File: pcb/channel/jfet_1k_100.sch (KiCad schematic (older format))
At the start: 7 parts, among them Q15 2SK3557-7-TB-E

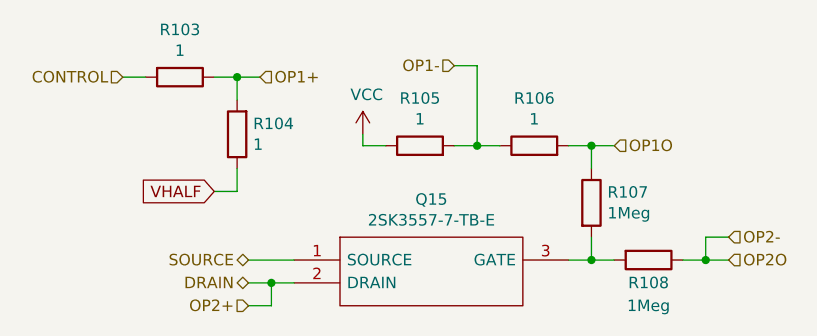
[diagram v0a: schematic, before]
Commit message: Reduce JFET base resistor from 1Meg to 100K
Precaution against too much voltage drop to base
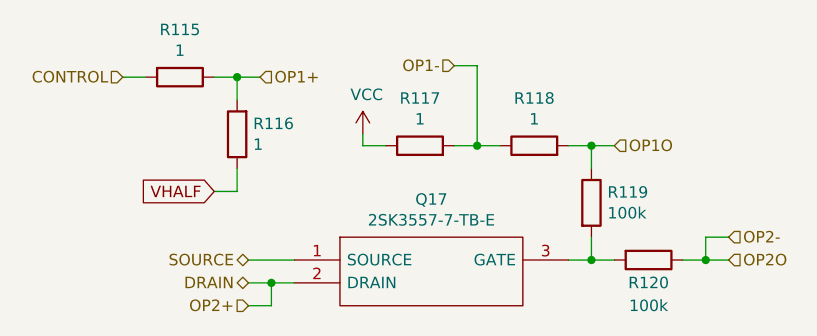
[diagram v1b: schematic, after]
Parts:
- R107, R108: value 1Meg -> 100k
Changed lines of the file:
@@
 $Descr A4 11693 8268
 encoding utf-8
-Sheet 17 19
+Sheet 18 19
 Title ""
 Date ""
@@
 Comment4 ""
 $EndDescr
-Wire Wire Line
-	6500 3950 6400 3950
-$Comp
-L Device:R R?
-U 1 1 5F3CFF6E
-P 6250 3950
-AR Path="/5F23B5B7/5F329280/5F32989F/5F3CFF6E" Ref="R?"  Part="1"
-AR Path="/5F23B5B7/5F329280/5F359E3D/5F3CFF6E" Ref="R?"  Part="1"
-AR Path="/5F23B5B7/5F329280/5F36404F/5F3CFF6E" Ref="R?"  Part="1"
-AR Path="/5F23B5B7/5F53A760/5F32989F/5F3CFF6E" Ref="R?"  Part="1"
-AR Path="/5F23B5B7/5F53A760/5F36404F/5F3CFF6E" Ref="R?"  Part="1"
-AR Path="/5F23B5B7/5F53A760/5F359E3D/5F3CFF6E" Ref="R?"  Part="1"
-AR Path="/5F23B5B7/5F53B8BF/5F32989F/5F3CFF6E" Ref="R?"  Part="1"
-AR Path="/5F23B5B7/5F53B8BF/5F36404F/5F3CFF6E" Ref="R?"  Part="1"
-AR Path="/5F23B5B7/5F53B8BF/5F359E3D/5F3CFF6E" Ref="R?"  Part="1"
-AR Path="/5F23B5B7/5F53BC28/5F32989F/5F3CFF6E" Ref="R?"  Part="1"
-AR Path="/5F23B5B7/5F53BC28/5F36404F/5F3CFF6E" Ref="R?"  Part="1"
-AR Path="/5F23B5B7/5F53BC28/5F359E3D/5F3CFF6E" Ref="R?"  Part="1"
-AR Path="/604ABC92/5F32989F/5F3CFF6E" Ref="R106"  Part="1"
-AR Path="/604ABC92/5F36404F/5F3CFF6E" Ref="R112"  Part="1"
-AR Path="/604ABC92/5F359E3D/5F3CFF6E" Ref="R118"  Part="1"
-F 0 "R106" V 6457 3950 50  0000 C CNN
-F 1 "1" V 6366 3950 50  0000 C CNN
-F 2 "Resistor_SMD:R_0603_1608Metric_Pad1.05x0.95mm_HandSolder" V 6180 3950 50  0001 C CNN
-F 3 "~" H 6250 3950 50  0001 C CNN
-	1    6250 3950
-	0    -1   -1   0
-$EndComp
-Wire Wire Line
-	6000 3950 6100 3950
-Connection ~ 6000 3950
 Wire Wire Line
 	5900 3950 6000 3950
@@
 AR Path="/604ABC92/5F36404F/5F3CF1A6" Ref="R111"  Part="1"
 AR Path="/604ABC92/5F359E3D/5F3CF1A6" Ref="R117"  Part="1"
-F 0 "R105" V 5957 3950 50  0000 C CNN
+F 0 "R117" V 5957 3950 50  0000 C CNN
 F 1 "1" V 5866 3950 50  0000 C CNN
 F 2 "Resistor_SMD:R_0603_1608Metric_Pad1.05x0.95mm_HandSolder" V 5680 3950 50  0001 C CNN
@@
 AR Path="/604ABC92/5F36404F/5F3D5B39" Ref="R114"  Part="1"
 AR Path="/604ABC92/5F359E3D/5F3D5B39" Ref="R120"  Part="1"
-F 0 "R108" V 6850 4450 50  0000 C CNN
-F 1 "1Meg" V 6950 4450 50  0000 C CNN
+F 0 "R120" V 6850 4450 50  0000 C CNN
+F 1 "100k" V 6950 4450 50  0000 C CNN
 F 2 "Resistor_SMD:R_0603_1608Metric_Pad1.05x0.95mm_HandSolder" V 6680 4450 50  0001 C CNN
 F 3 "~" H 6750 4450 50  0001 C CNN
@@
 Wire Wire Line
 	6500 4350 6500 4450
-$Comp
-L Device:R R?
-U 1 1 5F3D481C
-P 6500 4200
-AR Path="/5F23B5B7/5F329280/5F32989F/5F3D481C" Ref="R?"  Part="1"
-AR Path="/5F23B5B7/5F329280/5F359E3D/5F3D481C" Ref="R?"  Part="1"
-AR Path="/5F23B5B7/5F329280/5F36404F/5F3D481C" Ref="R?"  Part="1"
-AR Path="/5F23B5B7/5F53A760/5F32989F/5F3D481C" Ref="R?"  Part="1"
-AR Path="/5F23B5B7/5F53A760/5F36404F/5F3D481C" Ref="R?"  Part="1"
-AR Path="/5F23B5B7/5F53A760/5F359E3D/5F3D481C" Ref="R?"  Part="1"
-AR Path="/5F23B5B7/5F53B8BF/5F32989F/5F3D481C" Ref="R?"  Part="1"
-AR Path="/5F23B5B7/5F53B8BF/5F36404F/5F3D481C" Ref="R?"  Part="1"
-AR Path="/5F23B5B7/5F53B8BF/5F359E3D/5F3D481C" Ref="R?"  Part="1"
-AR Path="/5F23B5B7/5F53BC28/5F32989F/5F3D481C" Ref="R?"  Part="1"
-AR Path="/5F23B5B7/5F53BC28/5F36404F/5F3D481C" Ref="R?"  Part="1"
-AR Path="/5F23B5B7/5F53BC28/5F359E3D/5F3D481C" Ref="R?"  Part="1"
-AR Path="/604ABC92/5F32989F/5F3D481C" Ref="R107"  Part="1"
-AR Path="/604ABC92/5F36404F/5F3D481C" Ref="R113"  Part="1"
-AR Path="/604ABC92/5F359E3D/5F3D481C" Ref="R119"  Part="1"
-F 0 "R107" H 6570 4246 50  0000 L CNN
-F 1 "1Meg" H 6570 4155 50  0000 L CNN
-F 2 "Resistor_SMD:R_0603_1608Metric_Pad1.05x0.95mm_HandSolder" V 6430 4200 50  0001 C CNN
-F 3 "~" H 6500 4200 50  0001 C CNN
-	1    6500 4200
-	1    0    0    -1
-$EndComp
-Connection ~ 6500 3950
-Wire Wire Line
-	6500 4050 6500 3950
-Wire Wire Line
-	6600 3950 6500 3950
 $Comp
 L 2SK3557-7-TB-E:2SK3557-7-TB-E Q?
@@
 AR Path="/604ABC92/5F36404F/5F3D9719" Ref="Q16"  Part="1"
 AR Path="/604ABC92/5F359E3D/5F3D9719" Ref="Q17"  Part="1"
-F 0 "Q15" H 5800 4715 50  0000 C CNN
+F 0 "Q17" H 5800 4715 50  0000 C CNN
 F 1 "2SK3557-7-TB-E" H 5800 4624 50  0000 C CNN
 F 2 "footprints:SOT95P250X135-3N" H 6250 4550 50  0001 L CNN
@@
 AR Path="/604ABC92/5F36404F/5F3EDDFB" Ref="R110"  Part="1"
 AR Path="/604ABC92/5F359E3D/5F3EDDFB" Ref="R116"  Part="1"
-F 0 "R104" H 4880 3854 50  0000 R CNN
+F 0 "R116" H 4880 3854 50  0000 R CNN
 F 1 "1" H 4880 3945 50  0000 R CNN
 F 2 "Resistor_SMD:R_0603_1608Metric_Pad1.05x0.95mm_HandSolder" V 4880 3900 50  0001 C CNN
@@
 AR Path="/604ABC92/5F36404F/5F3EDDFA" Ref="R109"  Part="1"
 AR Path="/604ABC92/5F359E3D/5F3EDDFA" Ref="R115"  Part="1"
-F 0 "R103" V 4493 3650 50  0000 C CNN
+F 0 "R115" V 4493 3650 50  0000 C CNN
 F 1 "1" V 4584 3650 50  0000 C CNN
 F 2 "Resistor_SMD:R_0603_1608Metric_Pad1.05x0.95mm_HandSolder" V 4630 3650 50  0001 C CNN
@@
 AR Path="/604ABC92/5F36404F/60A3EF81" Ref="#PWR089"  Part="1"
 AR Path="/604ABC92/5F359E3D/60A3EF81" Ref="#PWR090"  Part="1"
-F 0 "#PWR089" H 5500 3750 50  0001 C CNN
+F 0 "#PWR090" H 5500 3750 50  0001 C CNN
 F 1 "VCC" H 5517 4073 50  0000 C CNN
 F 2 "" H 5500 3900 50  0001 C CNN
@@
 Wire Wire Line
 	6000 3600 6000 3950
+Connection ~ 6000 3950
+Wire Wire Line
+	6600 3950 6500 3950
+Wire Wire Line
+	6500 4050 6500 3950
+Connection ~ 6500 3950
+$Comp
+L Device:R R?
+U 1 1 5F3D481C
+P 6500 4200
+AR Path="/5F23B5B7/5F329280/5F32989F/5F3D481C" Ref="R?"  Part="1"
+AR Path="/5F23B5B7/5F329280/5F359E3D/5F3D481C" Ref="R?"  Part="1"
+AR Path="/5F23B5B7/5F329280/5F36404F/5F3D481C" Ref="R?"  Part="1"
+AR Path="/5F23B5B7/5F53A760/5F32989F/5F3D481C" Ref="R?"  Part="1"
+AR Path="/5F23B5B7/5F53A760/5F36404F/5F3D481C" Ref="R?"  Part="1"
+AR Path="/5F23B5B7/5F53A760/5F359E3D/5F3D481C" Ref="R?"  Part="1"
+AR Path="/5F23B5B7/5F53B8BF/5F32989F/5F3D481C" Ref="R?"  Part="1"
+AR Path="/5F23B5B7/5F53B8BF/5F36404F/5F3D481C" Ref="R?"  Part="1"
+AR Path="/5F23B5B7/5F53B8BF/5F359E3D/5F3D481C" Ref="R?"  Part="1"
+AR Path="/5F23B5B7/5F53BC28/5F32989F/5F3D481C" Ref="R?"  Part="1"
+AR Path="/5F23B5B7/5F53BC28/5F36404F/5F3D481C" Ref="R?"  Part="1"
+AR Path="/5F23B5B7/5F53BC28/5F359E3D/5F3D481C" Ref="R?"  Part="1"
+AR Path="/604ABC92/5F32989F/5F3D481C" Ref="R107"  Part="1"
+AR Path="/604ABC92/5F36404F/5F3D481C" Ref="R113"  Part="1"
+AR Path="/604ABC92/5F359E3D/5F3D481C" Ref="R119"  Part="1"
+F 0 "R119" H 6570 4246 50  0000 L CNN
+F 1 "100k" H 6570 4155 50  0000 L CNN
+F 2 "Resistor_SMD:R_0603_1608Metric_Pad1.05x0.95mm_HandSolder" V 6430 4200 50  0001 C CNN
+F 3 "~" H 6500 4200 50  0001 C CNN
+	1    6500 4200
+	1    0    0    -1
+$EndComp
+Wire Wire Line
+	6000 3950 6100 3950
+$Comp
+L Device:R R?
+U 1 1 5F3CFF6E
+P 6250 3950
+AR Path="/5F23B5B7/5F329280/5F32989F/5F3CFF6E" Ref="R?"  Part="1"
+AR Path="/5F23B5B7/5F329280/5F359E3D/5F3CFF6E" Ref="R?"  Part="1"
+AR Path="/5F23B5B7/5F329280/5F36404F/5F3CFF6E" Ref="R?"  Part="1"
+AR Path="/5F23B5B7/5F53A760/5F32989F/5F3CFF6E" Ref="R?"  Part="1"
+AR Path="/5F23B5B7/5F53A760/5F36404F/5F3CFF6E" Ref="R?"  Part="1"
+AR Path="/5F23B5B7/5F53A760/5F359E3D/5F3CFF6E" Ref="R?"  Part="1"
+AR Path="/5F23B5B7/5F53B8BF/5F32989F/5F3CFF6E" Ref="R?"  Part="1"
+AR Path="/5F23B5B7/5F53B8BF/5F36404F/5F3CFF6E" Ref="R?"  Part="1"
+AR Path="/5F23B5B7/5F53B8BF/5F359E3D/5F3CFF6E" Ref="R?"  Part="1"
+AR Path="/5F23B5B7/5F53BC28/5F32989F/5F3CFF6E" Ref="R?"  Part="1"
+AR Path="/5F23B5B7/5F53BC28/5F36404F/5F3CFF6E" Ref="R?"  Part="1"
+AR Path="/5F23B5B7/5F53BC28/5F359E3D/5F3CFF6E" Ref="R?"  Part="1"
+AR Path="/604ABC92/5F32989F/5F3CFF6E" Ref="R106"  Part="1"
+AR Path="/604ABC92/5F36404F/5F3CFF6E" Ref="R112"  Part="1"
+AR Path="/604ABC92/5F359E3D/5F3CFF6E" Ref="R118"  Part="1"
+F 0 "R118" V 6457 3950 50  0000 C CNN
+F 1 "1" V 6366 3950 50  0000 C CNN
+F 2 "Resistor_SMD:R_0603_1608Metric_Pad1.05x0.95mm_HandSolder" V 6180 3950 50  0001 C CNN
+F 3 "~" H 6250 3950 50  0001 C CNN
+	1    6250 3950
+	0    -1   -1   0
+$EndComp
+Wire Wire Line
+	6500 3950 6400 3950
 $EndSCHEMATC
